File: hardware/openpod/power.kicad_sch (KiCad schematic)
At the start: 21 parts

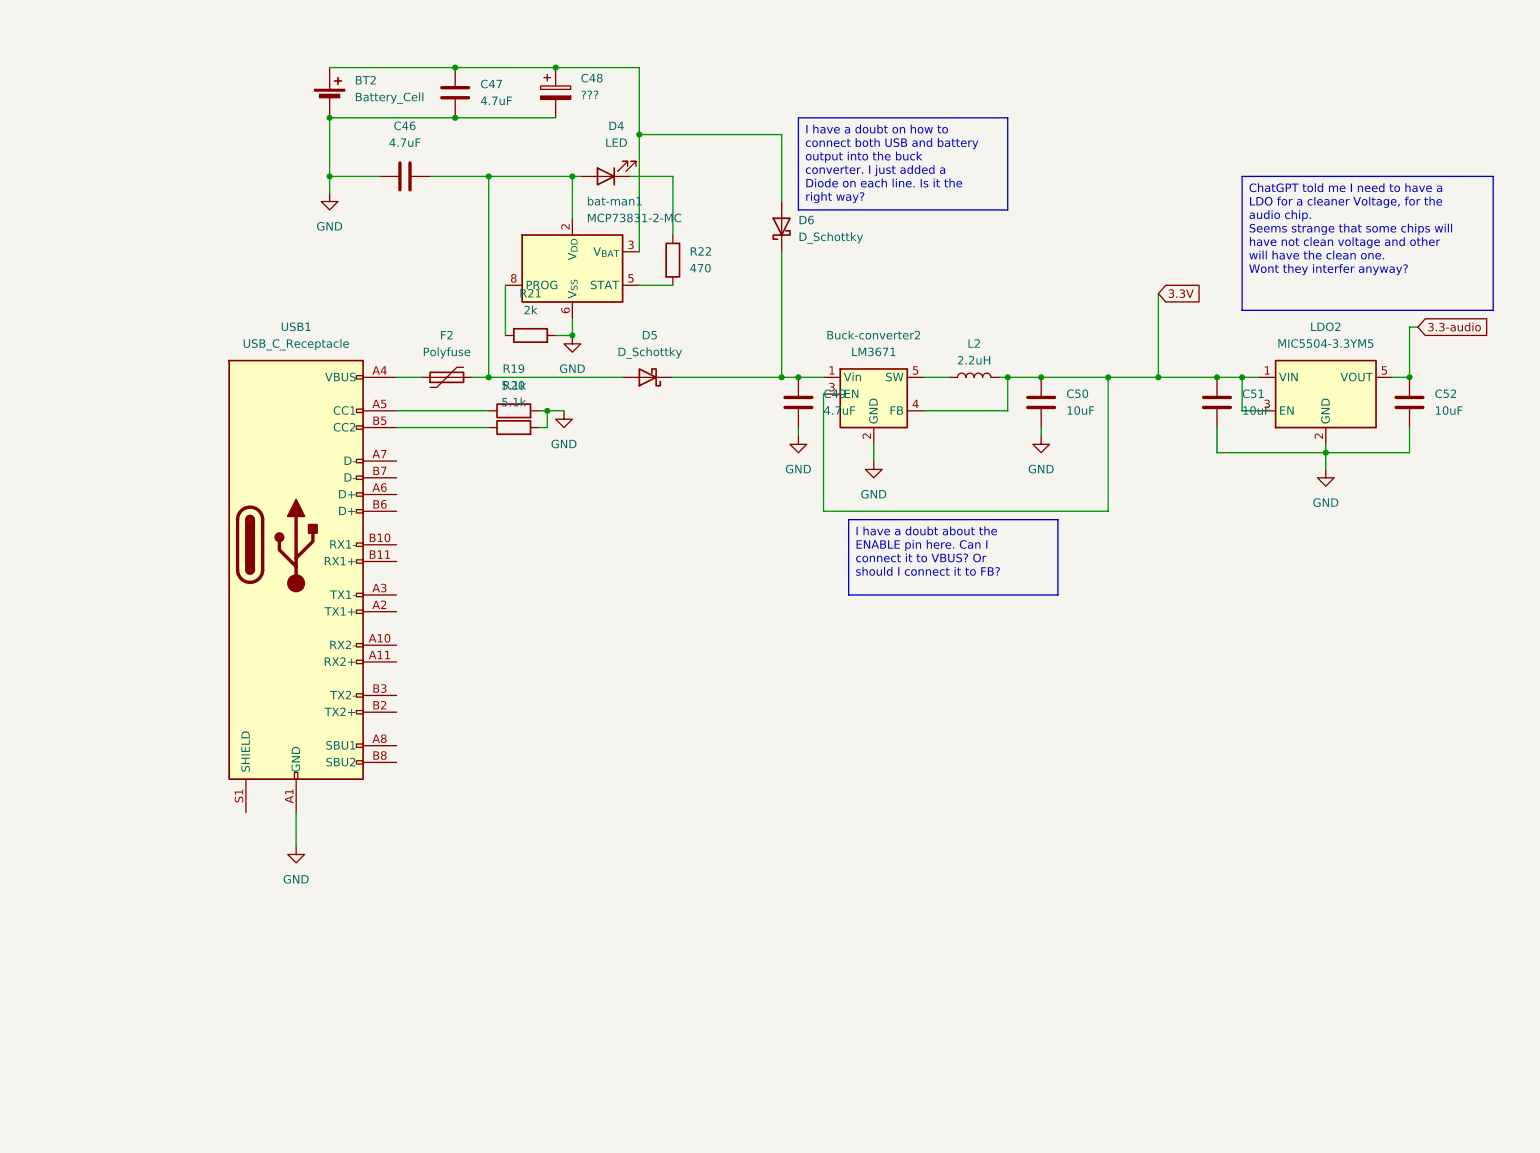
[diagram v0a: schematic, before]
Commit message: Rebirth (#2)
* designed clickwheel and see if mpr121 can fit on it

* update power and audio

* added UART converter

* added bluetooth

* try up with vs1053 feather

* setupt the player file

* fill screen with different colors

* almost works with GFX, just wrong coordinates

* test MADCTL 1

* wrong, screen is all white

* screen pins before remap

* new pinout with consecutive 16bits on the PCs pins

* screen works

* added demo

* updated platformio.ini

* added blog

* cleanup

* first menu

* Fast (ugly) menu renderer

* ugly theme + blog post

* transition using HW scrolling

* breakdown ui

* 30 rows buffer

* remove row/col shit

* added content for the blog

* start restoring render of the now playing

* scroll to nowplaying

* working transitiontotracklist (but slight prolbem with last line)

* fixed the wrapping issue at the bottom

* update theme

* rewired vs1053

* screen and mp3 working

* pins

* updated mp3 pinout to have i2c available

* testing the clickwheel with teleplot: looking good !

* Debugging the wheel: it follows my finger on the screen

* first scrolling the tracks with the wheel !

* WIP

* use an app state and allow to use more bits per pixel

* setup unit tests

* std

* remove select track

* use doctest and reporter

* make tests pass

* cleanup

* fixed scripts

* faster render fonts

* dark background

* better state + events handler system

* wip

* faster renderer of tracklist + animations + better split between concerns

* 2 bits per pixel

* docs

* remove unit tests

* simplify ui list

* rename track to element

* rename track to element

* psram controller

* psram works on SPI1

* psram controller works

* indexer

* crawler

* radix tree?

* update trie generator

* started implementing storage

* trie index

* search works on the stm32

* can retrieve now paths

* sound player on the way

* enhanced mp3 working, but not flac

* flac plugin

* config files

* load flac plugin correctly: saccaded sound

* cleaning up

*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
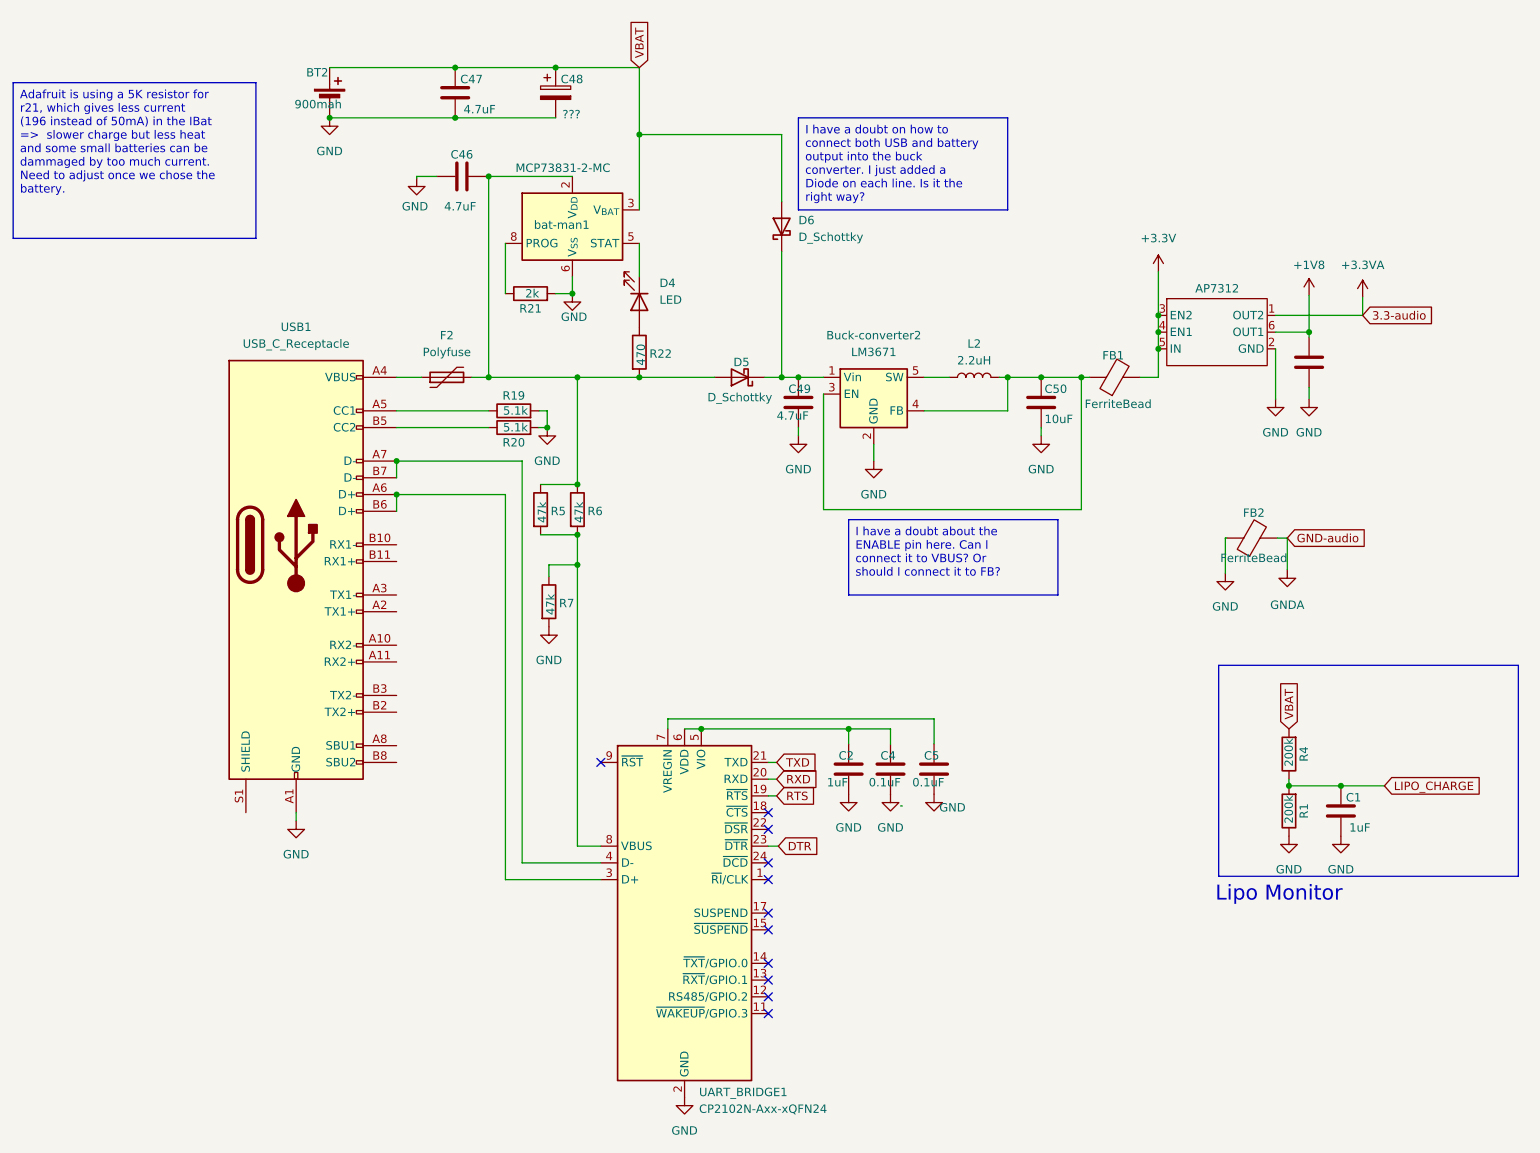
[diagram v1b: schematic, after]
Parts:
- removed C51: 10uF, symbol Device:C
- removed LDO2: MIC5504-3.3YM5, Package_TO_SOT_SMD:SOT-23-5, symbol Regulator_Linear:MIC5504-3.3YM5
- added AP7312: ~, Package_TO_SOT_SMD:SOT-23-6, symbol openpod:AP7312
- added C1, C2: 1uF, symbol Device:C
- added C4, C5: 0.1uF, symbol Device:C
- added FB1, FB2: FerriteBead, symbol Device:FerriteBead
- added R1, R4: 200k, symbol Device:R
- added R5, R6, R7: 47k, symbol Device:R
- added UART_BRIDGE1: CP2102N-Axx-xQFN24, Package_DFN_QFN:QFN-24-1EP_4x4mm_P0.5mm_EP2.6x2.6mm, symbol Interface_USB:CP2102N-Axx-xQFN24
- BT2: value Battery_Cell -> 900mah; Part number (none) -> LP053450
- C52: value 10uF -> 1uF
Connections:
- net GND: now also AP7312.2 (GND), C1.2, C2.2, C4.2, C5.2, FB2.1, R1.1, R7.2, UART_BRIDGE1.2 (GND), UART_BRIDGE1.25 (GND)
- net at D4.1 (K): now also bat-man1.5 (STAT); no longer R22.1
- net at C46.2, D5.2 (A), F2.2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: now also R22.2, R5.1, R6.1; no longer D4.2 (A)
- net VBAT: now reaches BT2.1 (+), C47.1, C48.1, D6.2 (A), bat-man1.3 (V_{BAT}), bat-man1.4 (V_{BAT})
- net VBAT: now also R4.2
- net at USB1.A6 (D+): now also USB1.B6 (D+), UART_BRIDGE1.3 (D+)
- net at USB1.A7 (D-): now also USB1.B7 (D-), UART_BRIDGE1.4 (D-)
- net 3.3-audio renamed +1V8
- net +1V8: now also AP7312.6 (OUT1)
- net 3.3V: no longer names the net of Buck-converter2.3 (EN), Buck-converter2.4 (FB), C50.1, L2.2
- net 3.3V: now also FB1.1
- new net: D4.2 (A), R22.1
- new net: C2.1, C4.1, UART_BRIDGE1.5 (VIO), UART_BRIDGE1.6 (VDD)
- new net: C5.1, UART_BRIDGE1.7 (VREGIN)
- new net: R5.2, R6.2, R7.1, UART_BRIDGE1.8 (VBUS)
- new net +3.3V: AP7312.3 (EN2), AP7312.4 (EN1), AP7312.5 (IN), FB1.2
- new net +3.3VA: AP7312.1 (OUT2)
- new net DTR: UART_BRIDGE1.23 (~{DTR})
- new net GNDA: FB2.2
- new net LIPO_CHARGE: C1.1, R1.2, R4.1
- new net RTS: UART_BRIDGE1.19 (~{RTS})
- new net RXD: UART_BRIDGE1.20 (RXD)
- new net TXD: UART_BRIDGE1.21 (TXD)
- no-connect marks 0 -> 11
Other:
- note added: "Lipo Monitor"
- moved on the sheet: C46, D4, D5, R21, R22, bat-man1
